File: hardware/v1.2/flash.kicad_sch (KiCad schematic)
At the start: 10 parts, among them U1 ECP5-CABGA256, U11 W25Q128JVS

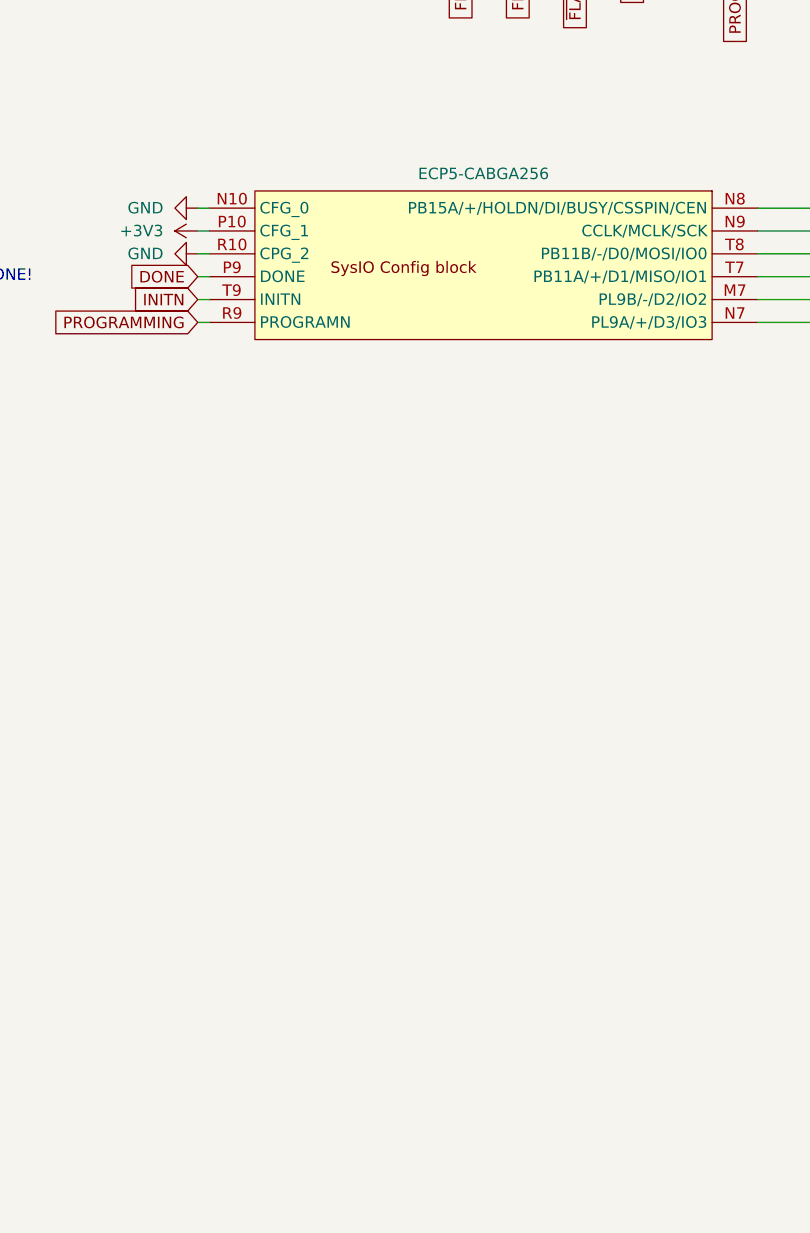
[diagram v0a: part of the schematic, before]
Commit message: UART to PS2 converter
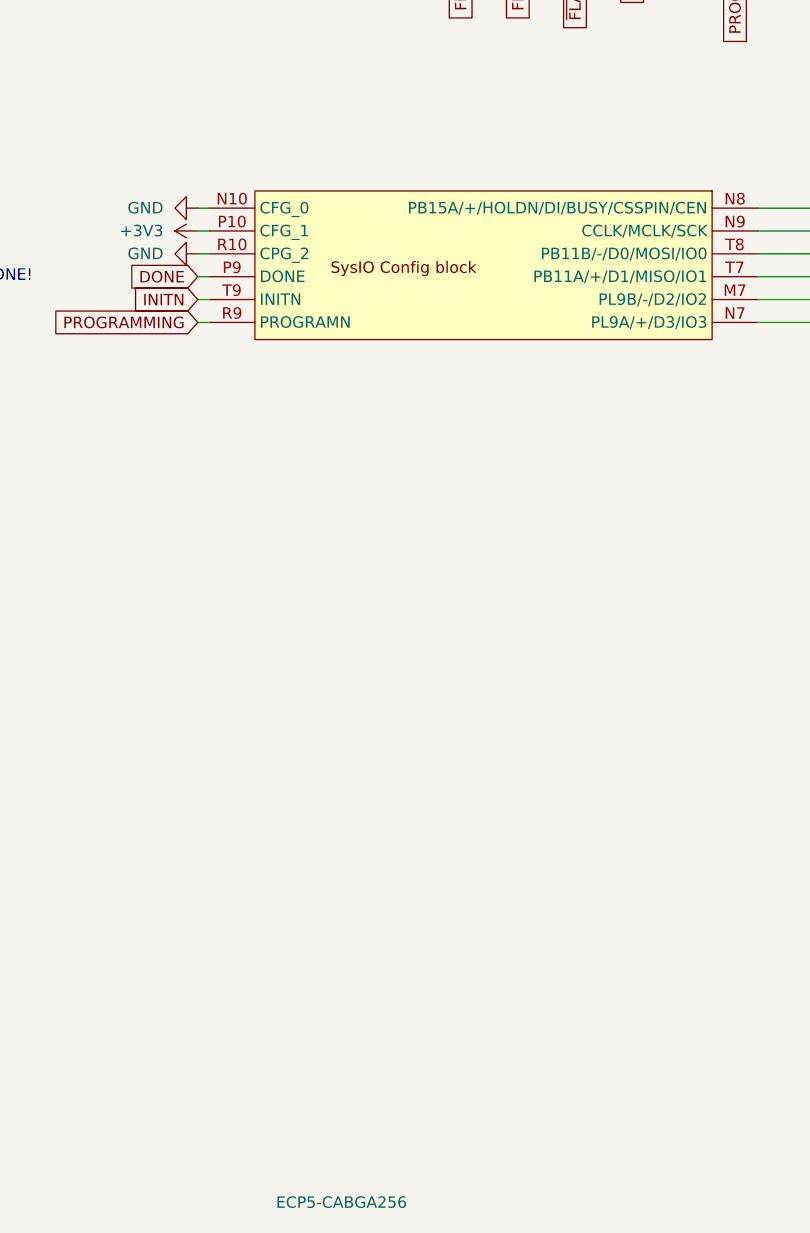
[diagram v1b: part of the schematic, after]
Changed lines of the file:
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@@
 		)
 		(property "Value" "ECP5-CABGA256"
-			(at 115.57 105.41 0)
+			(at 107.0767 219.71 0)
 			(effects
 				(font
 					(size 1.27 1.27)
 				)
+				(justify left)
 			)
 		)
@@
 		)
 		(instances
-			(project "icepi-zero"
+			(project ""
+				(path "/f88da08e-cf42-4d03-a08f-3f602fe6658d/17c9c9b3-f379-4e1f-a876-d3fcf0529a4d"
+					(reference "U1")
+					(unit 3)
+				)
 				(path "/f88da08e-cf42-4d03-a08f-3f602fe6658d/d4e07380-5584-4eac-bd07-d260a33e64d7"
 					(reference "U1")
